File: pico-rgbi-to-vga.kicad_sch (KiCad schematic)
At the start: 25 parts, among them J1 SDS-80J, J2 DB15_Female_HighDensity, J3 USB-B1HSB6, SW1 SW_Push, U1 Pico

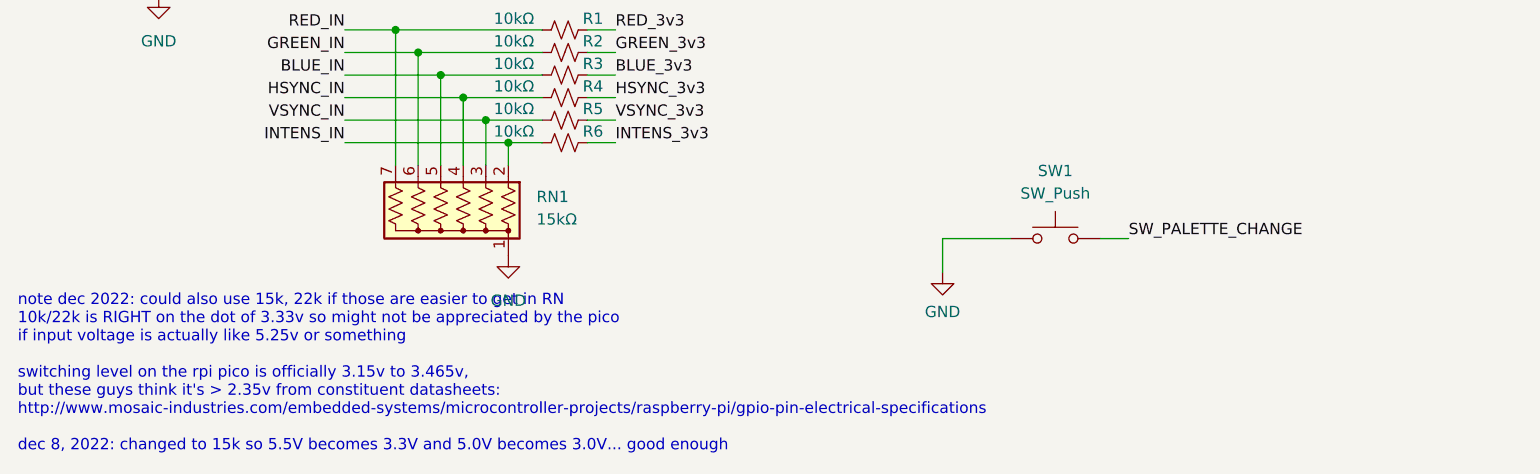
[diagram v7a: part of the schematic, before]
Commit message: Use 8SIP for Vdiv pulldown, 7SIP is not available
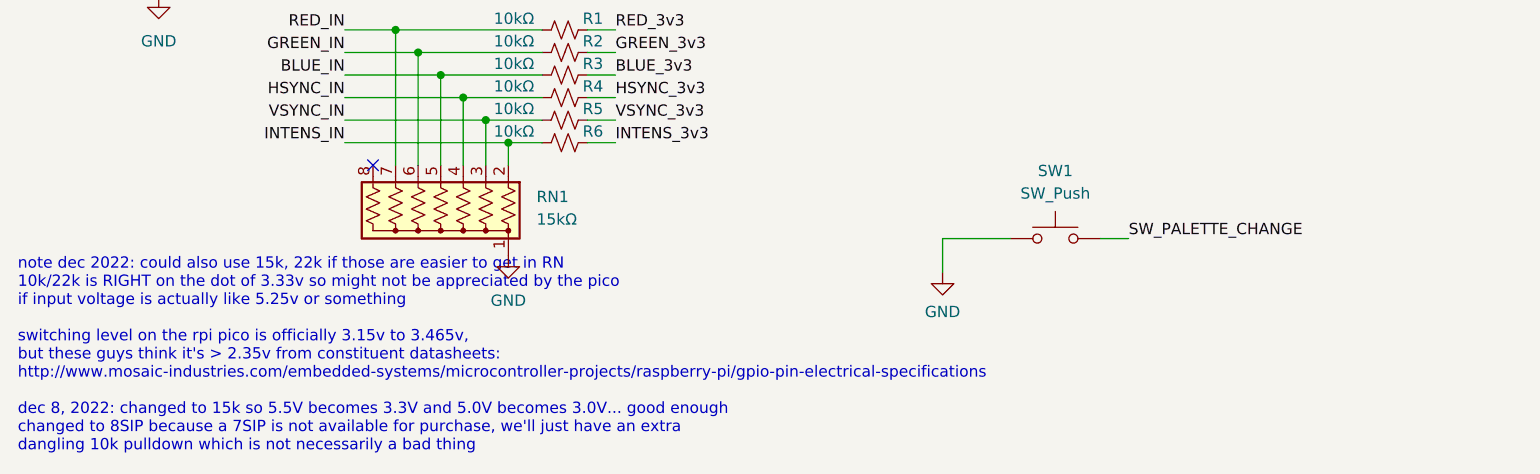
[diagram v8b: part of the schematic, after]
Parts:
- removed RN1: 15kΩ, Resistor_THT:R_Array_SIP7, symbol Device:R_Network06_US
- added RN1: 15kΩ, Resistor_THT:R_Array_SIP8, symbol Device:R_Network07_US
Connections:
- net BLUE_IN: now also RN1.5 (R4)
- net GND: now also RN1.1 (common)
- net GREEN_IN: now also RN1.6 (R5)
- net HSYNC_IN: now also RN1.4 (R3)
- net INTENS_IN: now also RN1.2 (R1)
- net RED_IN: now also RN1.7 (R6)
- net VSYNC_IN: now also RN1.3 (R2)
- no-connect marks 7 -> 8
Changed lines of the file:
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@@
   (junction (at 242.57 24.765) (diameter 0) (color 0 0 0 0)
   )
+  (no_connect (at 56.515 146.05))
   (no_connect (at 230.505 127.635))
   (no_connect (at 42.545 29.845))
@@
     (effects (font (size 1.27 1.27)) (justify left bottom))
   )
-  (text "note dec 2022: could also use 15k, 22k if those are easier to get in RN\n10k/22k is RIGHT on the dot of 3.33v so might not be appreciated by the pico\nif input voltage is actually like 5.25v or something\n\nswitching level on the rpi pico is officially 3.15v to 3.465v,\nbut these guys think it's > 2.35v from constituent datasheets:\nhttp://www.mosaic-industries.com/embedded-systems/microcontroller-projects/raspberry-pi/gpio-pin-electrical-specifications\n\ndec 8, 2022: changed to 15k so 5.5V becomes 3.3V and 5.0V becomes 3.0V... good enough"
+  (text "note dec 2022: could also use 15k, 22k if those are easier to get in RN\n10k/22k is RIGHT on the dot of 3.33v so might not be appreciated by the pico\nif input voltage is actually like 5.25v or something\n\nswitching level on the rpi pico is officially 3.15v to 3.465v,\nbut these guys think it's > 2.35v from constituent datasheets:\nhttp://www.mosaic-industries.com/embedded-systems/microcontroller-projects/raspberry-pi/gpio-pin-electrical-specifications\n\ndec 8, 2022: changed to 15k so 5.5V becomes 3.3V and 5.0V becomes 3.0V... good enough\nchanged to 8SIP because a 7SIP is not available for purchase, we'll just have an extra\ndangling 10k pulldown which is not necessarily a bad thing"
     (at 16.51 178.435 0)
     (effects (font (size 1.27 1.27)) (justify left bottom))
@@
     (pin "2")
   )
+  (symbol (lib_id "Device:R_Network07_US") (at 64.135 151.13 180) (unit 1)
+    (in_bom yes) (on_board yes) (fields_autoplaced)
+    (property "Reference" "RN1" (id 0) (at 74.93 149.6059 0)
+      (effects (font (size 1.27 1.27)) (justify right))
+    )
+    (property "Value" "15kΩ" (id 1) (at 74.93 152.1459 0)
+      (effects (font (size 1.27 1.27)) (justify right))
+    )
+    (property "Footprint" "Resistor_THT:R_Array_SIP8" (id 2) (at 52.07 151.13 90)
+      (effects (font (size 1.27 1.27)) hide)
+    )
+    (property "Datasheet" "http://www.vishay.com/docs/31509/csc.pdf" (id 3) (at 64.135 151.13 0)
+      (effects (font (size 1.27 1.27)) hide)
+    )
+    (pin "1")
+    (pin "2")
+    (pin "3")
+    (pin "4")
+    (pin "5")
+    (pin "6")
+    (pin "7")
+    (pin "8")
+  )
   (symbol (lib_id "Jumper:Jumper_2_Bridged") (at 49.53 93.345 0) (unit 1)
     (in_bom yes) (on_board yes)
@@
     (pin "1")
   )
-  (symbol (lib_id "Device:R_Network06_US") (at 64.135 151.13 180) (unit 1)
-    (in_bom yes) (on_board yes) (fields_autoplaced)
-    (property "Reference" "RN1" (id 0) (at 74.93 149.6059 0)
-      (effects (font (size 1.27 1.27)) (justify right))
-    )
-    (property "Value" "15kΩ" (id 1) (at 74.93 152.1459 0)
-      (effects (font (size 1.27 1.27)) (justify right))
-    )
-    (property "Footprint" "Resistor_THT:R_Array_SIP7" (id 2) (at 54.61 151.13 90)
-      (effects (font (size 1.27 1.27)) hide)
-    )
-    (property "Datasheet" "http://www.vishay.com/docs/31509/csc.pdf" (id 3) (at 64.135 151.13 0)
-      (effects (font (size 1.27 1.27)) hide)
-    )
-    (property "Mouser" "652-4607X-1LF-22K" (id 5) (at 64.135 151.13 0)
-      (effects (font (size 1.27 1.27)) hide)
-    )
-    (pin "1")
-    (pin "2")
-    (pin "3")
-    (pin "4")
-    (pin "5")
-    (pin "6")
-    (pin "7")
-  )
   (symbol (lib_id "USB-B1HSB6:USB-B1HSB6") (at 40.005 29.845 0) (mirror y) (unit 1)
     (in_bom yes) (on_board yes) (fields_autoplaced)
@@
       (reference "R16") (unit 1) (value "100Ω") (footprint "Resistor_SMD:R_0805_2012Metric_Pad1.20x1.40mm_HandSolder")
     )
-    (path "/dcda6a74-0460-40e6-8ee3-a792f5780acc"
-      (reference "RN1") (unit 1) (value "15kΩ") (footprint "Resistor_THT:R_Array_SIP7")
+    (path "/35ecf34e-5f7a-4f6f-a41b-4b72b19a0d36"
+      (reference "RN1") (unit 1) (value "15kΩ") (footprint "Resistor_THT:R_Array_SIP8")
     )
     (path "/3ebb7414-8370-4606-bcb1-2b26f5893364"
